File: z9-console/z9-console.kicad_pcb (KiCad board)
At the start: 2 copper layers, 89.5 x 55.5 mm, 128 parts, among them J10 Screw_Terminal_01x06, J2 LCD 3.2" 240x320 Conn_01x14_P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, J4 Conn_01x04_Pin, J6 ST_STDC14 - SAMTEC_FTSH-107-0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, J7 TC2070 - TAG Connect, J801 USB_C_Receptacle_USB2.0_16P, J9 JST GH, Q701 AO3400A, SW2 SW_Push, SW3 SW_Push, U2 TPS22919DCKR, U3 SN74LVC1G14DRLR, U301 TLV76733DRVx, U303 LMR14006YDDCR, U8 STM32F427V_G-I_Tx, U9 ISM330DHCX, U951 ISO1042-Q1, U952 B0505XT-1WR3, X2 8MHz 20pF

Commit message: x
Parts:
- added C82501: 10uF, PCM_JLCPCB:C_0603, F.Cu at (57.9, 67.5)
- added C82502: 10uF, PCM_JLCPCB:C_0603, F.Cu at (57.9, 69.8)
- added C82503: 100nF, dnt:C_0603_1608Metric, F.Cu at (54.0, 67.7)
- added C82504: 10uF, dnt:C_0603_1608Metric, F.Cu at (54.0, 70.2)
- added F82501: Fuse_16V_500mA_100A_1A_150mΩ_0805_PTC, Fuse:Fuse_0805_2012Metric, F.Cu at (49.8, 67.9)
- added J82501: USB_C_Receptacle_USB2.0_16P, Connector_USB:USB_C_Receptacle_G-Switch_GT-USB-7051x, F.Cu at (42.1, 70.1)
- added R82501: 100kΩ, PCM_JLCPCB:R_0603, F.Cu at (59.2, 45.9)
- added R82502: 100kΩ, PCM_JLCPCB:R_0603, F.Cu at (59.2, 48.2)
- added R82503: 47Ω, PCM_JLCPCB:R_0603, F.Cu at (59.2, 50.4)
- added R82504: 5.1kΩ, PCM_JLCPCB:R_0402, F.Cu at (58.8, 55.5)
- added R82505: 5.1kΩ, PCM_JLCPCB:R_0402, F.Cu at (58.8, 57.4)
- added R82506: 5.1kΩ, PCM_JLCPCB:R_0402, F.Cu at (58.8, 59.2)
- added TP82501: PE0, TestPoint:TestPoint_Pad_D1.0mm, F.Cu at (58.9, 53.1)
- added U82501: TLV76733DRVx, Package_SON:WSON-6-1EP_2x2mm_P0.65mm_EP1x1.6mm_ThermalVias, F.Cu at (49.5, 71.2)
- added U82502: ESP32-S3-WROOM-1, PCM_Espressif:ESP32-S3-WROOM-1U, F.Cu at (114.9, 117.3)
- moved R2 20.5 mm to (92.3, 113.7)
- moved R22 15.0 mm to (113.2, 105.0)
- moved TP39 14.3 mm to (111.2, 106.6)
- moved R23 13.0 mm to (117.9, 105.5)
- moved U2 10.6 mm to (94.2, 116.4)
- moved R3 4.22 mm to (92.6, 111.2)
- moved TP37 3.75 mm to (102.3, 107.8)
- moved TP18 1.75 mm to (126.0, 111.1)
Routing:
- net /SPI2_IRQ: track 80.8 -> 40.4 mm, vias 6 -> 4
- net /SPI4_CS_2: track 91.9 -> 76.8 mm
- net /SPI2_IRQ2: track 84.2 -> 72.2 mm, vias 3 -> 2
- net Net-(J2-VCC): track 50.1 -> 42.4 mm, vias 5 -> 3
- net /LCD_ON: track 59.0 -> 54.4 mm
- net /MCU/PA1: track 18.3 -> 14.2 mm, vias 2 -> 1
- net /MCU/NRST: track 71.6 -> 74.9 mm
- net +3.3V: track 439.6 -> 436.4 mm
- net /SPI2_SDO: track 50.0 -> 46.9 mm
- net /SPI2_CS: track 49.1 -> 47.4 mm
- net /SPI2_SCK: track 68.4 -> 67.4 mm
- net /SYS_WAKEUP: track 25.2 -> 24.7 mm, vias 4 -> 2
- net GND: vias 504 -> 474

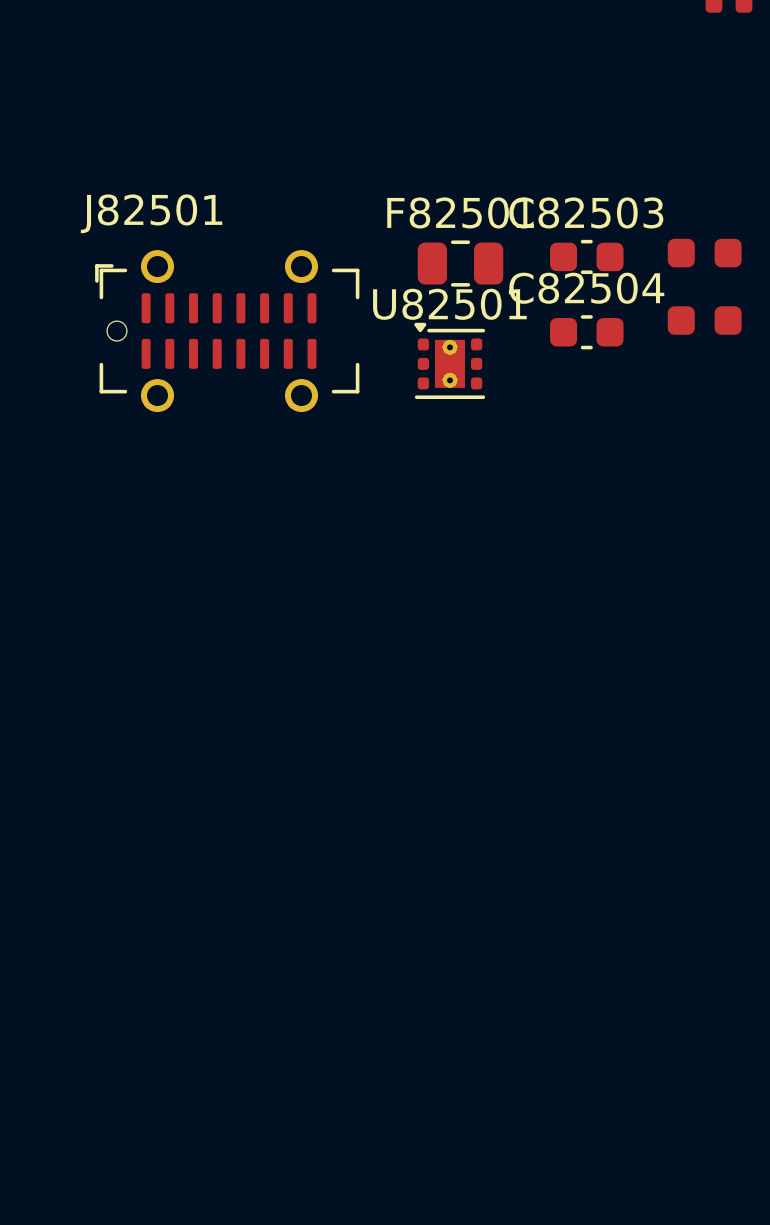
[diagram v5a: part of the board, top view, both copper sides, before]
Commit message: Update KiCad project and schematic files for z9-console - Changed project UUID in z9-console.kicad_pro to a new unique identifier. - Updated schematic version from 20250114 to 20260306 and generator version from 9.0 to 10.0 in z9-console.kicad_sch. - Modified date in title block to 2026-04-29. - Added properties for components to control visibility and autoplace behavior. - Ensured all mounting holes have consistent properties for reference, value, footprint, and description. - Updated project references in instances to match the new project name. - Cleaned up color properties in fill elements to ensure proper rendering.
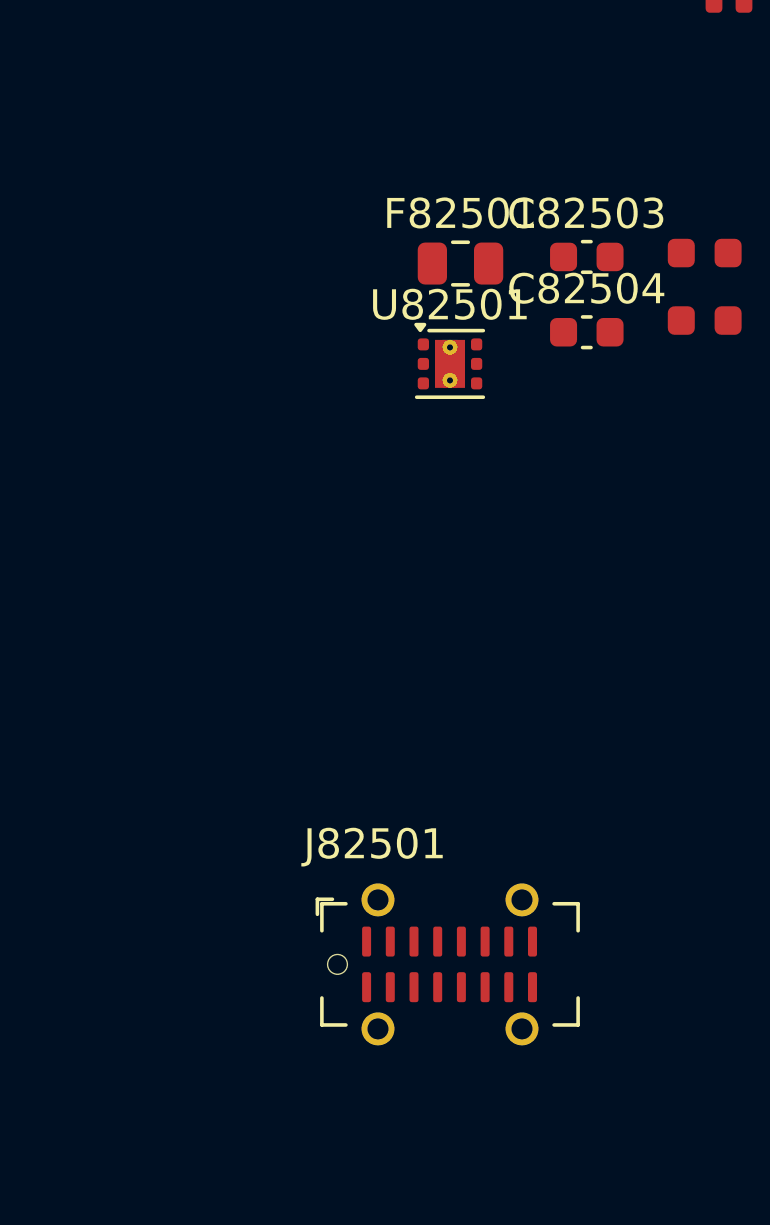
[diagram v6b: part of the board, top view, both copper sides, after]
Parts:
- moved J82501 22.4 mm to (49.5, 91.2)
